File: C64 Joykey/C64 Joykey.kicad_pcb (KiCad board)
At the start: 2 copper layers, 99.7 x 74.9 mm, 29 parts, among them J1 Port_1, J2 Port_2, M1 Mounting, M2 Mounting, M3 Mounting, M4 Mounting, SW1 FIRE1, SW2 FIRE2, SW3 FIRE3, SW4 UP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

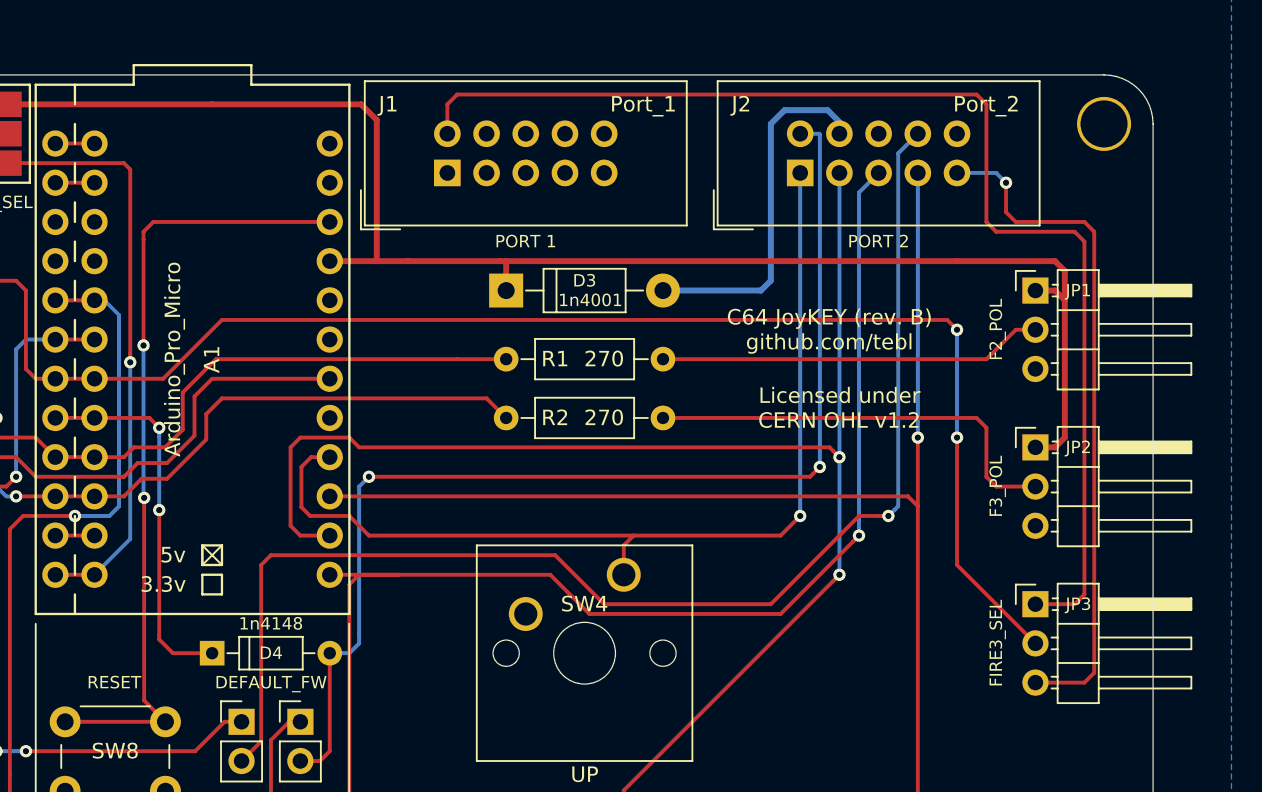
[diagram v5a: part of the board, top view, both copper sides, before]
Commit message: Swapped jumper layout (need new pictures)
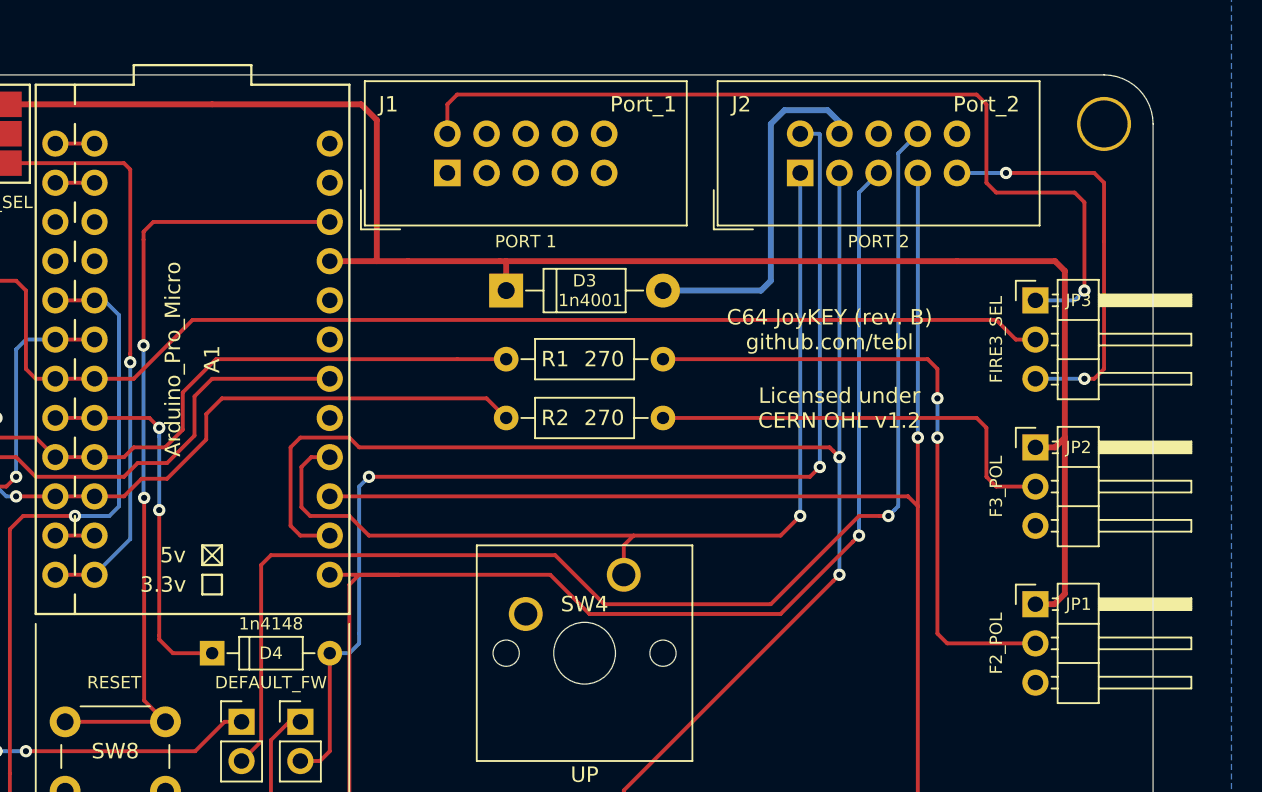
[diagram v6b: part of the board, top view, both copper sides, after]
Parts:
- moved JP1 20.3 mm to (233.0, 116.8)
- moved JP3 19.7 mm to (233.0, 97.2)
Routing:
- net P1_FIRE1: track 78.2 -> 58.5 mm, vias 0 -> 1
- net P2_FIRE3: track 44.2 -> 26.6 mm, vias 1 -> 2
- net /FIRE3_IN: track 100.0 -> 82.9 mm, vias 2 -> 0
- net Net-(JP1-Pad2): track 24.9 -> 41.8 mm, vias 0 -> 2
- net VCC: track 98.5 -> 108.6 mm
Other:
- board text added: "FIRE3 SELECT"
- board text removed: "FIRE3 OUTPUT"

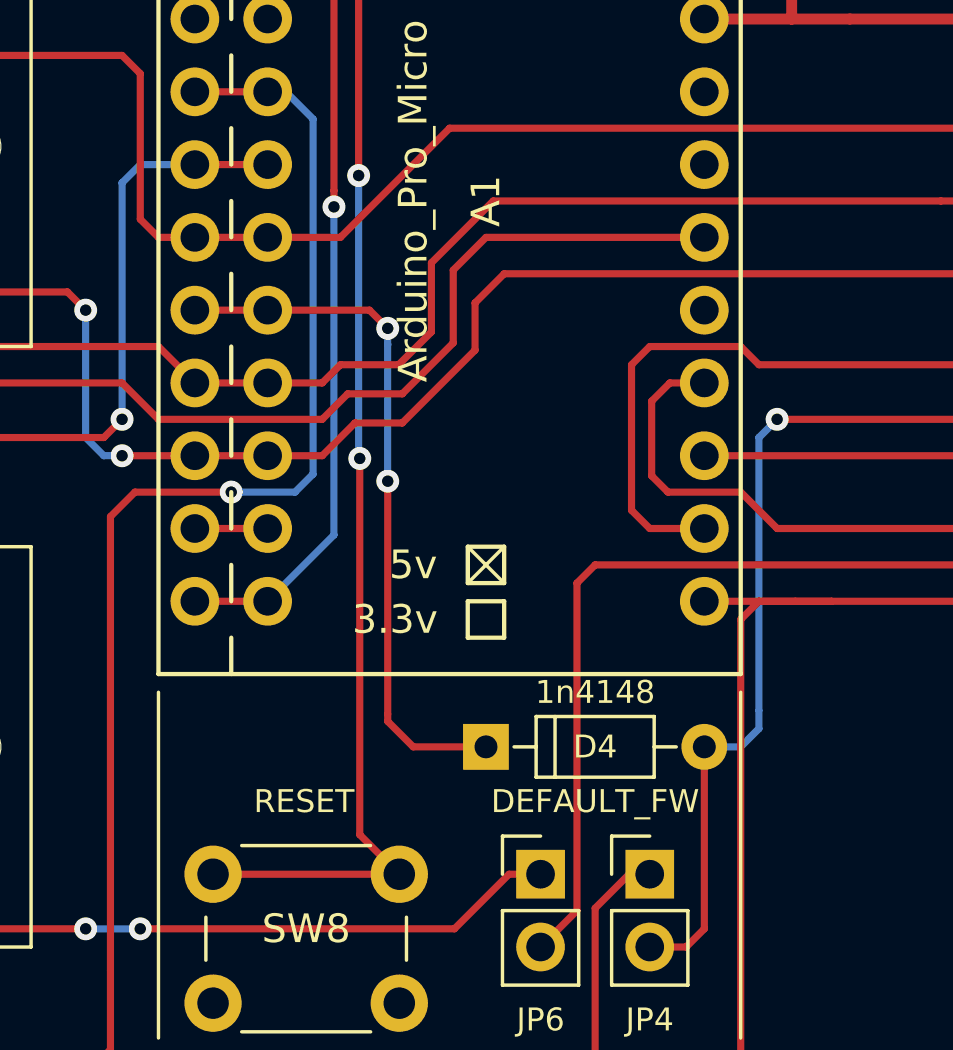
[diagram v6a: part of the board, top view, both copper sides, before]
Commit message: Added series resistor to output pin
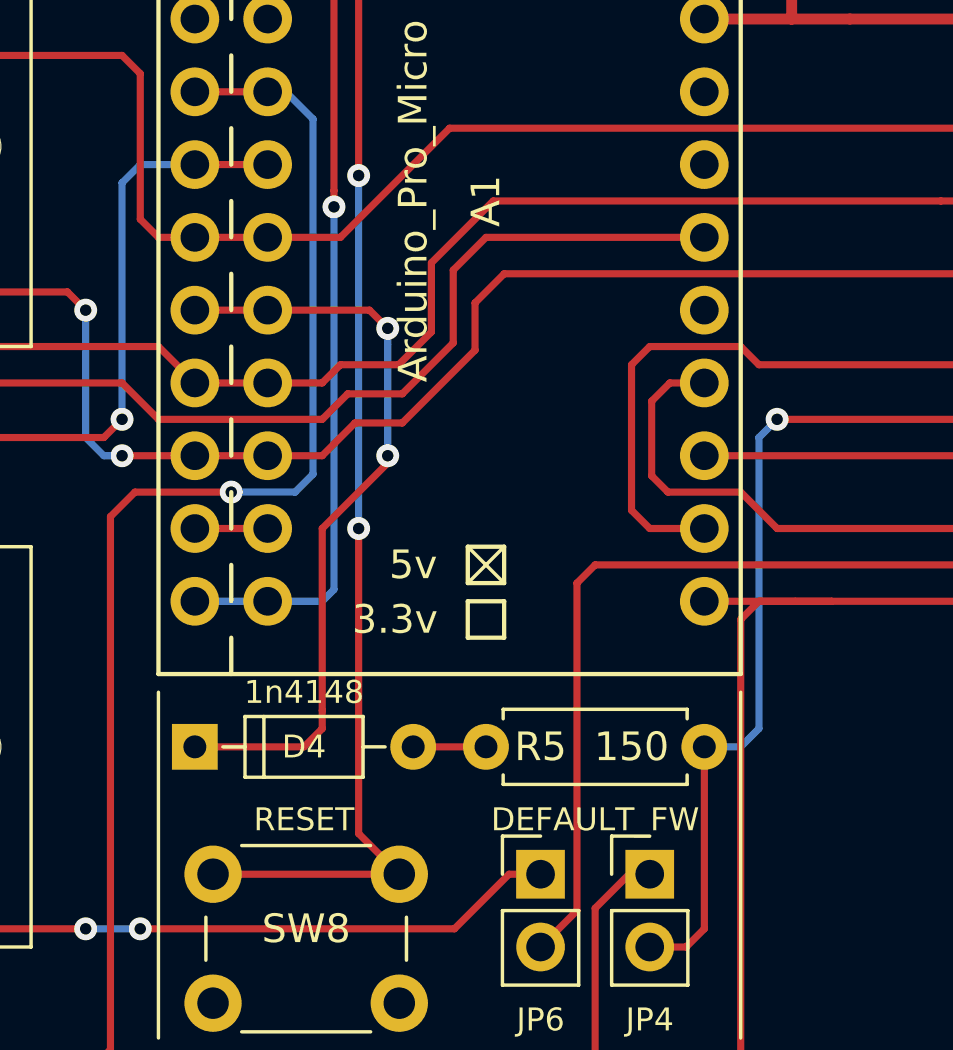
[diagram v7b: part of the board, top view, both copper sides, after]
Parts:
- added R5: 150, Resistors_THT:R_Axial_DIN0207_L6.3mm_D2.5mm_P7.62mm_Horizontal, F.Cu at (179.7, 120.0)
- moved D4 10.2 mm to (169.5, 120.0)
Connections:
- D4 pad 2: P2_FIRE1 -> Net-(D4-Pad2)
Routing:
- net Net-(D4-Pad2): track 0.00 -> 2.54 mm
- net /FIRE1_OUT: track 24.5 -> 26.6 mm
- net Net-(A1-Pad12): track 38.0 -> 39.1 mm

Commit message: Moved JP3
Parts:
- moved JP3 0.64 mm to (233.0, 96.5)
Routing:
- net P1_FIRE1: track 58.5 -> 57.8 mm
- net P2_FIRE3: track 26.6 -> 25.9 mm
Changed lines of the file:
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@@
     (thickness 1.6)
     (drawings 140)
-    (tracks 312)
+    (tracks 310)
     (zones 0)
     (modules 30)
@@
   )
   (module Pin_Headers:Pin_Header_Angled_1x03_Pitch2.54mm (layer F.Cu)
-    (at 233.045 97.155)
+    (at 233.045 96.52)
     (descr "Through hole angled pin header, 1x03, 2.54mm pitch, 6mm pin length, single row")
     (tags "Through hole angled pin header THT 1x03 2.54mm single row")
@@
   )
   (gr_line (start 234.95 105.41) (end 234.95 107.315) (layer B.SilkS) (width 0.12))
-  (gr_text "FIRE3\nSELECT" (at 239.395 99.695 90) (layer B.SilkS)
+  (gr_text "FIRE3\nSELECT" (at 239.395 99.06 90) (layer B.SilkS)
     (effects (font (size 0.8 0.8) (thickness 0.1)) (justify mirror))
   )
@@
   (gr_line (start 140.97 154.305) (end 140.97 85.725) (layer Edge.Cuts) (width 0.05))
   (gr_line (start 237.49 157.48) (end 144.145 157.48) (layer Edge.Cuts) (width 0.05))
-  (via (at 236.22 96.52) (size 0.8) (drill 0.4) (layers F.Cu B.Cu) (net 1))
-  (segment (start 236.22 96.52) (end 235.585 97.155) (width 0.25) (layer B.Cu) (net 1))
-  (segment (start 235.585 97.155) (end 233.045 97.155) (width 0.25) (layer B.Cu) (net 1))
+  (via (at 236.22 95.885) (size 0.8) (drill 0.4) (layers F.Cu B.Cu) (net 1))
+  (segment (start 233.045 96.52) (end 235.585 96.52) (width 0.25) (layer B.Cu) (net 1))
+  (segment (start 235.585 96.52) (end 236.22 95.885) (width 0.25) (layer B.Cu) (net 1))
+  (segment (start 235.585 90.17) (end 230.505 90.17) (width 0.25) (layer F.Cu) (net 1))
+  (segment (start 229.235 83.82) (end 195.58 83.82) (width 0.25) (layer F.Cu) (net 1))
+  (segment (start 229.87 89.535) (end 229.87 84.455) (width 0.25) (layer F.Cu) (net 1))
+  (segment (start 230.505 90.17) (end 229.87 89.535) (width 0.25) (layer F.Cu) (net 1))
+  (segment (start 229.87 84.455) (end 229.235 83.82) (width 0.25) (layer F.Cu) (net 1))
+  (segment (start 236.22 90.805) (end 235.585 90.17) (width 0.25) (layer F.Cu) (net 1))
+  (segment (start 195.58 83.82) (end 194.945 84.455) (width 0.25) (layer F.Cu) (net 1))
   (segment (start 194.945 84.455) (end 194.945 86.36) (width 0.25) (layer F.Cu) (net 1))
-  (segment (start 195.58 83.82) (end 194.945 84.455) (width 0.25) (layer F.Cu) (net 1))
-  (segment (start 229.235 83.82) (end 195.58 83.82) (width 0.25) (layer F.Cu) (net 1))
-  (segment (start 236.22 96.52) (end 236.22 90.805) (width 0.25) (layer F.Cu) (net 1))
-  (segment (start 229.87 84.455) (end 229.235 83.82) (width 0.25) (layer F.Cu) (net 1))
-  (segment (start 230.505 90.17) (end 229.87 89.535) (width 0.25) (layer F.Cu) (net 1))
-  (segment (start 236.22 90.805) (end 235.585 90.17) (width 0.25) (layer F.Cu) (net 1))
-  (segment (start 235.585 90.17) (end 230.505 90.17) (width 0.25) (layer F.Cu) (net 1))
-  (segment (start 229.87 89.535) (end 229.87 84.455) (width 0.25) (layer F.Cu) (net 1))
+  (segment (start 236.22 95.885) (end 236.22 90.805) (width 0.25) (layer F.Cu) (net 1))
   (via (at 223.52003 111.125) (size 0.8) (drill 0.4) (layers F.Cu B.Cu) (net 3))
   (segment (start 225.425 86.36) (end 224.155 87.63) (width 0.25) (layer B.Cu) (net 3) (status 10))
@@
   (segment (start 187.325 126.365) (end 187.325 120.015) (width 0.25) (layer F.Cu) (net 5))
   (segment (start 227.965 88.9) (end 230.505 88.9) (width 0.25) (layer B.Cu) (net 6) (status 10))
-  (segment (start 237.49 101.6) (end 237.49 93.345) (width 0.25) (layer F.Cu) (net 6))
   (via (at 231.14 88.9) (size 0.8) (drill 0.4) (layers F.Cu B.Cu) (net 6))
   (segment (start 230.505 88.9) (end 231.14 88.9) (width 0.25) (layer B.Cu) (net 6))
-  (segment (start 231.14 88.9) (end 236.855 88.9) (width 0.25) (layer F.Cu) (net 6))
-  (segment (start 237.49 89.535) (end 237.49 93.345) (width 0.25) (layer F.Cu) (net 6))
-  (segment (start 236.855 88.9) (end 237.49 89.535) (width 0.25) (layer F.Cu) (net 6))
-  (via (at 236.22 102.235) (size 0.8) (drill 0.4) (layers F.Cu B.Cu) (net 6))
-  (segment (start 233.045 102.235) (end 236.22 102.235) (width 0.25) (layer B.Cu) (net 6))
-  (segment (start 236.22 102.235) (end 236.855 102.235) (width 0.25) (layer F.Cu) (net 6))
-  (segment (start 236.855 102.235) (end 237.49 101.6) (width 0.25) (layer F.Cu) (net 6))
+  (via (at 236.22 101.6) (size 0.8) (drill 0.4) (layers F.Cu B.Cu) (net 6))
+  (segment (start 233.045 101.6) (end 236.22 101.6) (width 0.25) (layer B.Cu) (net 6))
+  (segment (start 236.855 88.9) (end 231.14 88.9) (width 0.25) (layer F.Cu) (net 6))
+  (segment (start 237.49 89.535) (end 236.855 88.9) (width 0.25) (layer F.Cu) (net 6))
+  (segment (start 237.49 100.965) (end 237.49 89.535) (width 0.25) (layer F.Cu) (net 6))
+  (segment (start 236.22 101.6) (end 236.855 101.6) (width 0.25) (layer F.Cu) (net 6))
+  (segment (start 236.855 101.6) (end 237.49 100.965) (width 0.25) (layer F.Cu) (net 6))
   (segment (start 187.325 109.855) (end 224.789994 109.855) (width 0.25) (layer F.Cu) (net 7) (status 10))
   (segment (start 224.789994 109.855) (end 224.79 109.855006) (width 0.25) (layer F.Cu) (net 7))
@@
   (segment (start 167.64 101.6) (end 168.275 102.235) (width 0.25) (layer F.Cu) (net 23))
   (segment (start 168.275 102.235) (end 169.545 102.235) (width 0.25) (layer F.Cu) (net 23) (status 20))
-  (segment (start 230.505 98.425) (end 231.775 99.695) (width 0.25) (layer F.Cu) (net 23))
-  (segment (start 178.435 98.425) (end 230.505 98.425) (width 0.25) (layer F.Cu) (net 23))
+  (segment (start 178.435 98.425) (end 232.41 98.425) (width 0.25) (layer F.Cu) (net 23))
   (segment (start 172.085 102.235) (end 174.625 102.235) (width 0.25) (layer F.Cu) (net 23))
-  (segment (start 231.775 99.695) (end 233.045 99.695) (width 0.25) (layer F.Cu) (net 23))
+  (segment (start 232.41 98.425) (end 233.045 99.06) (width 0.25) (layer F.Cu) (net 23))
   (segment (start 174.625 102.235) (end 178.435 98.425) (width 0.25) (layer F.Cu) (net 23))
   (segment (start 169.545 97.155) (end 172.085 97.155) (width 0.25) (layer F.Cu) (net 24) (status 30))
